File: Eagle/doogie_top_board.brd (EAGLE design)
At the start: 92.9 x 75 mm, 19 parts, among them T1 BC337, U1 RPI-ZERO, U2 U1V10F5, U3 GY-521MPU6050, U4 ADC-4CH-ADS1115, U5 74HC4051_SPARKFUN

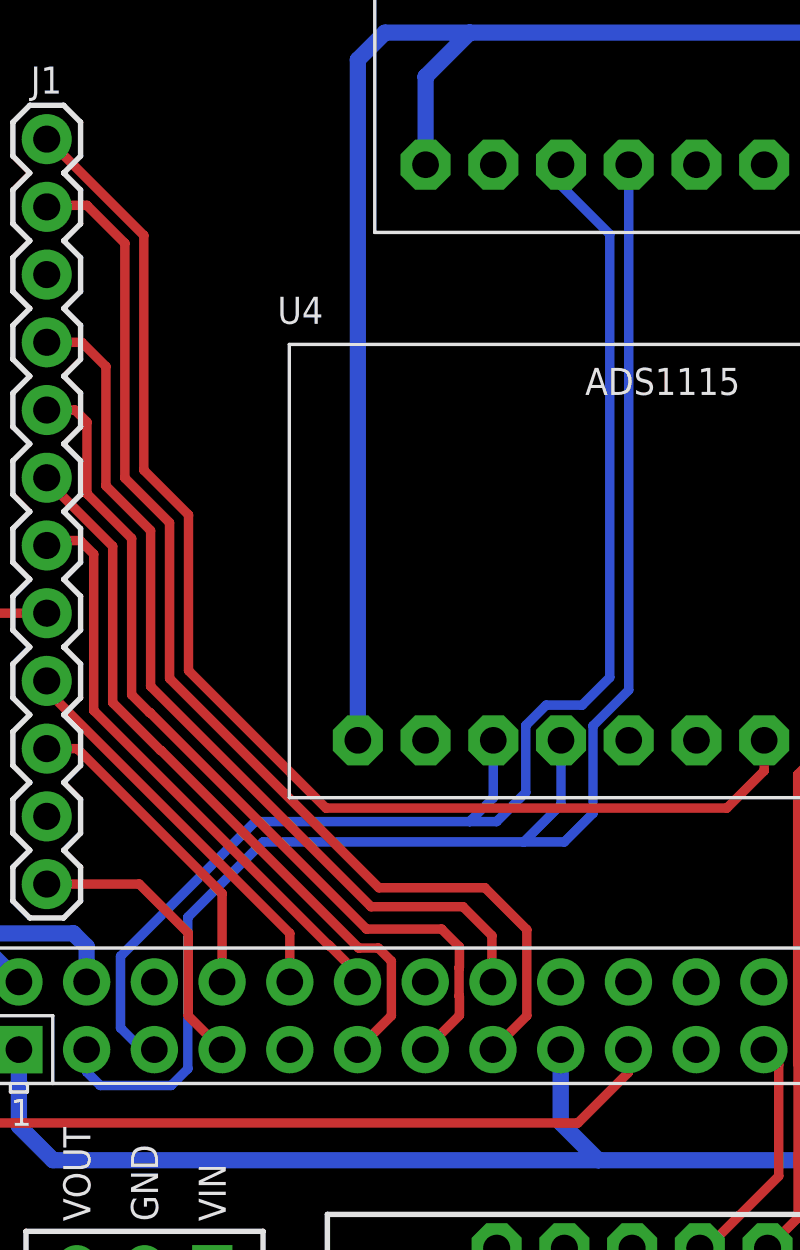
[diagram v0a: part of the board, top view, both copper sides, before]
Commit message: Fix copper traces of I2C bus
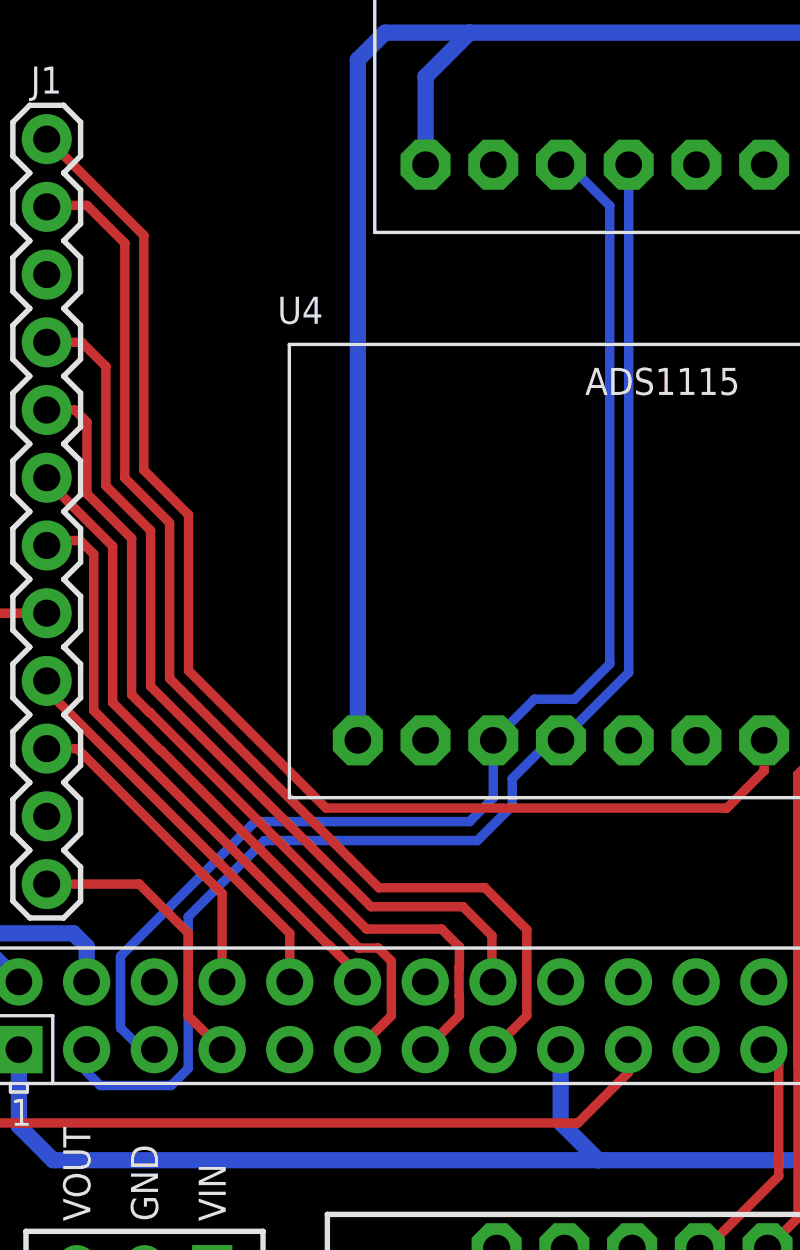
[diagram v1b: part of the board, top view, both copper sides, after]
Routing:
- net I2C_SDA: track 56.9 -> 50.8 mm
- net I2C_SCL: track 51.9 -> 48.1 mm
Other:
- board text removed: "/home/menezes/Pictures/BIR - logo (PB).bmp"
